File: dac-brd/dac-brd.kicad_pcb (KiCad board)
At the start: 4 copper layers, 59.5 x 87 mm, 27 parts, among them J1 I2C/1Wire, J2 UART, J3 STK1, J4 STK2, J5 STK3, J6 STK4, J7 LED, U1 REF5020ID, U2 DAC5578xPW, U3 DAC5578xPW

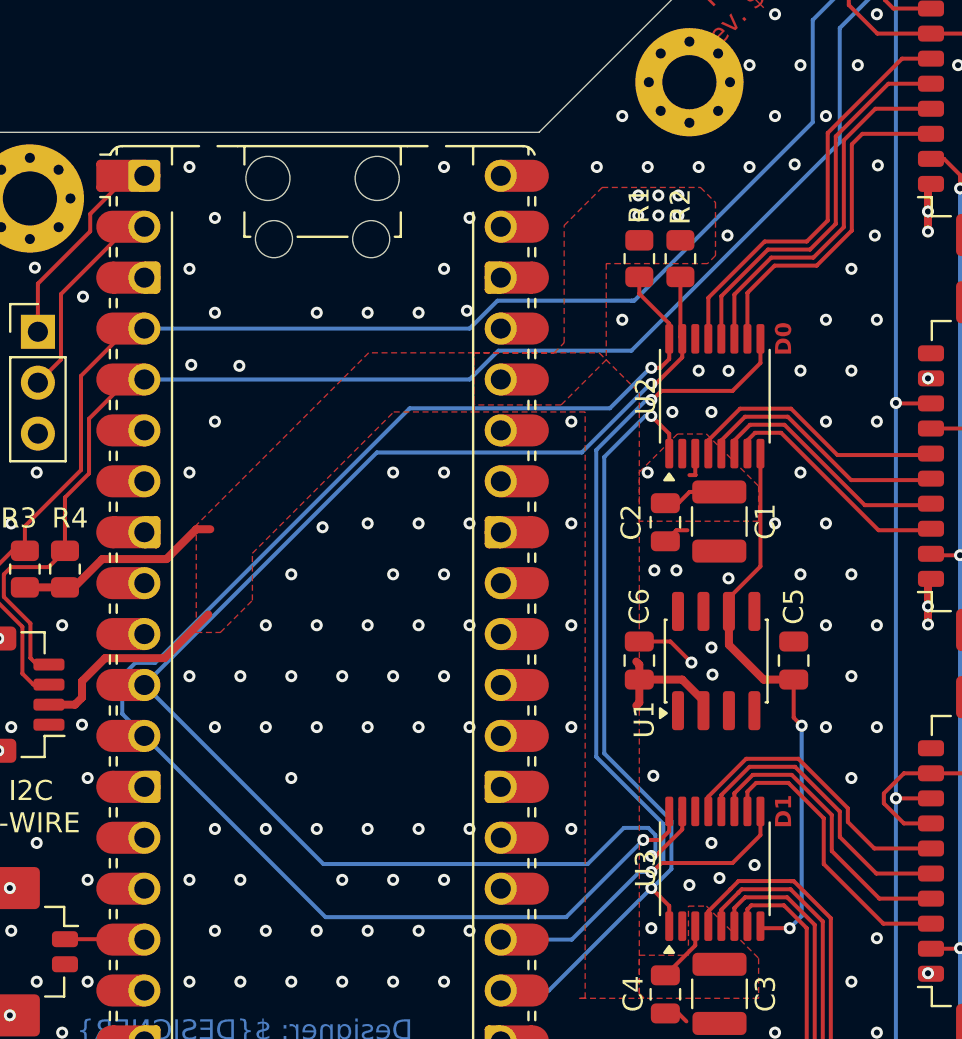
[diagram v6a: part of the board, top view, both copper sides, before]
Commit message: Indicate using rp2350a. Re-wire I2C0 connections on DAC board for easier layout
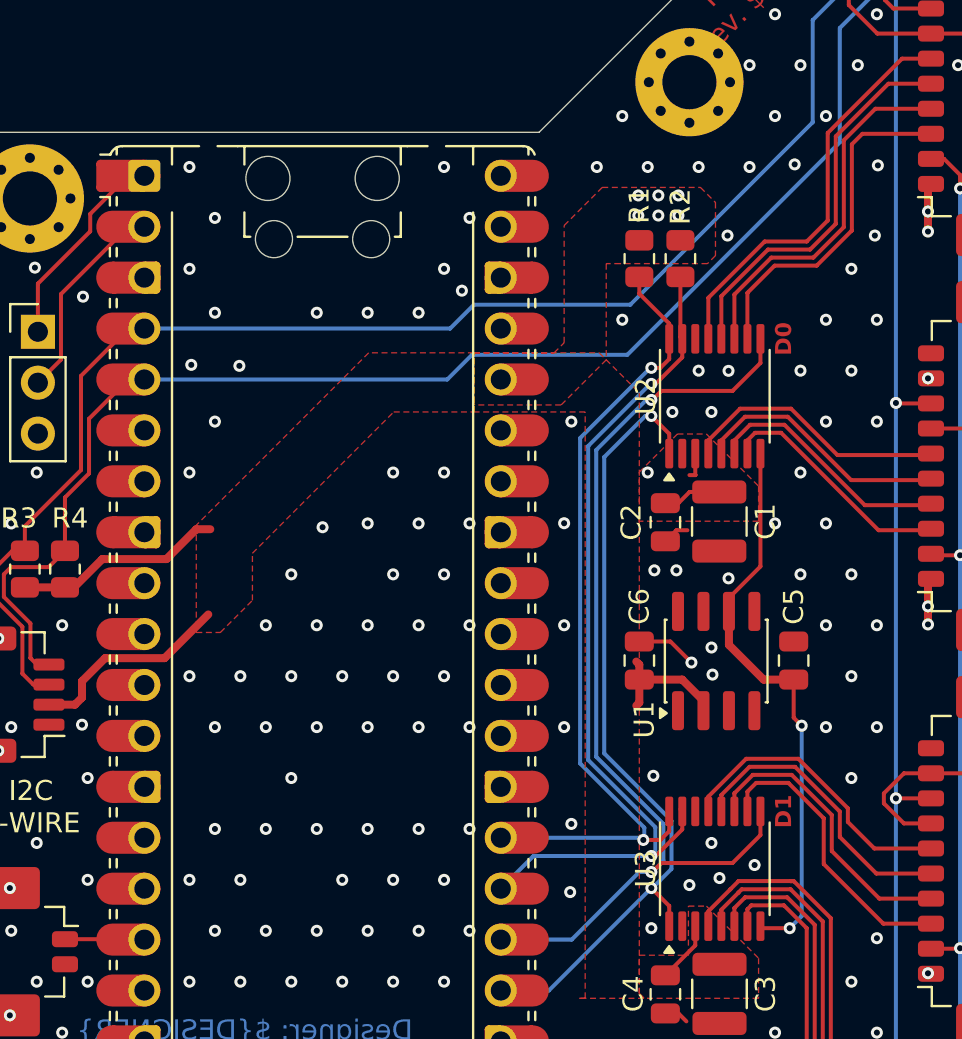
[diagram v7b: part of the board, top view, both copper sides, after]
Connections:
- A1 pad 11: /SDA -> unconnected-(A1-GPIO8-Pad11)
- A1 pad 12: /SCL -> unconnected-(A1-GPIO9-Pad12)_1
- A1 pad 26: unconnected-(A1-GPIO20-Pad26)_1 -> /SDA
- A1 pad 27: unconnected-(A1-GPIO21-Pad27) -> /SCL
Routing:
- net /SCL: track 74.7 -> 41.8 mm
- net /SDA: track 72.0 -> 43.8 mm
- net GND: vias 272 -> 273

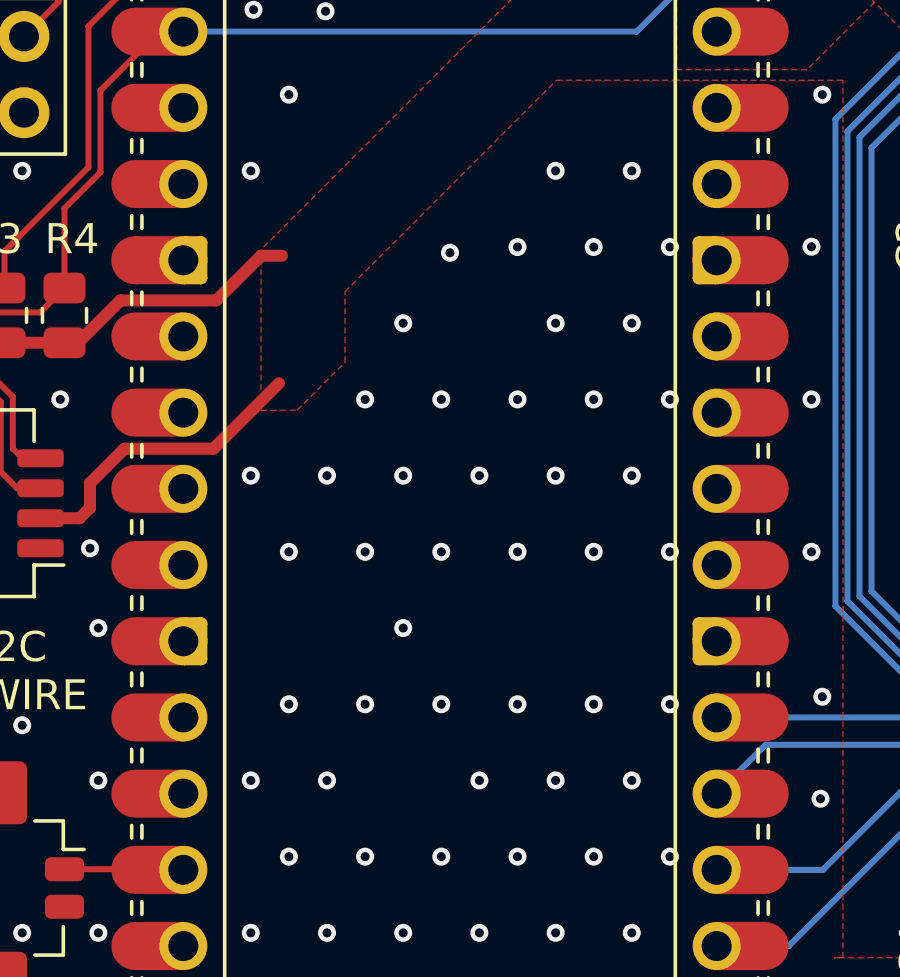
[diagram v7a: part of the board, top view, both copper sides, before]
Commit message: Adding power conditioning board
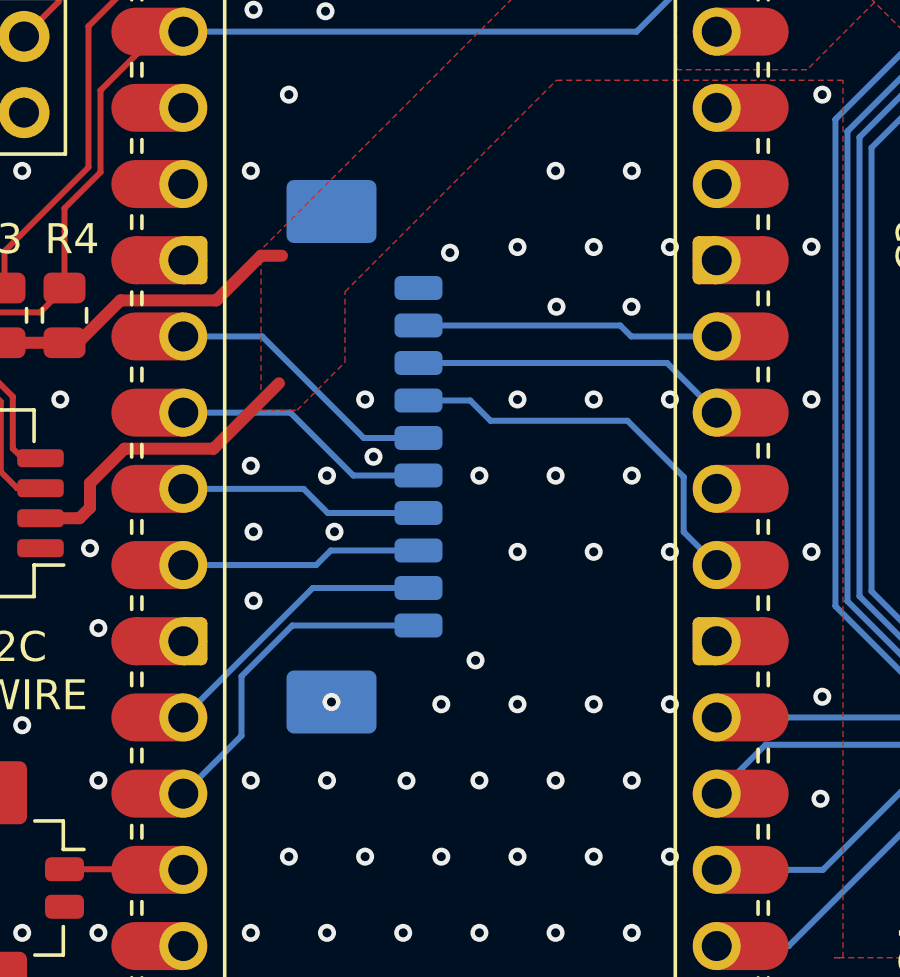
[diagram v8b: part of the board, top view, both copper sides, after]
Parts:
- added J8: PWRCTRL, Connector_Molex:Molex_PicoBlade_53261-1071_1x10-1MP_P1.25mm_Horizontal, B.Cu at (147.2, 104.5)
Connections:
- A1 pad 10: unconnected-(A1-GPIO7-Pad10) -> /ST2
- A1 pad 11: unconnected-(A1-GPIO8-Pad11) -> /SEL1
- A1 pad 12: unconnected-(A1-GPIO9-Pad12)_1 -> /SEL2
- A1 pad 14: unconnected-(A1-GPIO10-Pad14) -> /LATCH
- A1 pad 15: unconnected-(A1-GPIO11-Pad15) -> /DEN
- A1 pad 29: unconnected-(A1-GPIO22-Pad29)_1 -> /PWREN
- A1 pad 31: unconnected-(A1-GPIO26_ADC0-Pad31)_1 -> /ADC0
- A1 pad 32: unconnected-(A1-GPIO27_ADC1-Pad32)_1 -> /ADC1
- A1 pad 9: unconnected-(A1-GPIO6-Pad9) -> /ST1
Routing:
- net /PWREN: track 0.00 -> 13.3 mm
- net /DEN: track 0.00 -> 11.3 mm
- net /ADC0: track 0.00 -> 10.6 mm
- net /ADC1: track 0.00 -> 10.1 mm
- net /LATCH: track 0.00 -> 9.63 mm
- net /ST1: track 0.00 -> 9.24 mm
- net /ST2: track 0.00 -> 8.71 mm
- net /SEL1: track 0.00 -> 8.17 mm
- net /SEL2: track 0.00 -> 8.04 mm
- net GND: vias 273 -> 271
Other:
- board text added: "INRUSH LIMITER"
